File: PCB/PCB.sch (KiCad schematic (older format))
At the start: 32 parts, among them SW1 SW_Push, U1 ATmega32U4-AU, Y1 16MHz

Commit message: finished PCB?
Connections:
- net GND: now also USB1.6 (SHIELD)
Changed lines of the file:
@@
 L power:GND #PWR0113
 U 1 1 608FED04
-P 4750 2150
-F 0 "#PWR0113" H 4750 1900 50  0001 C CNN
-F 1 "GND" H 4755 1977 50  0000 C CNN
-F 2 "" H 4750 2150 50  0001 C CNN
-F 3 "" H 4750 2150 50  0001 C CNN
-	1    4750 2150
-	1    0    0    -1
-$EndComp
-Wire Wire Line
-	4450 2150 4750 2150
+P 5750 2150
+F 0 "#PWR0113" H 5750 1900 50  0001 C CNN
+F 1 "GND" H 5755 1977 50  0000 C CNN
+F 2 "" H 5750 2150 50  0001 C CNN
+F 3 "" H 5750 2150 50  0001 C CNN
+	1    5750 2150
+	1    0    0    -1
+$EndComp
 Text GLabel 2650 4900 0    50   Input ~ 0
 ROW1
@@
 	1    0    0    -1
 $EndComp
-$Comp
-L random-keyboard-parts:Molex-0548190589 USB1
-U 1 1 608F48FD
-P 4150 1950
-F 0 "USB1" V 4687 1917 60  0000 C CNN
-F 1 "Molex-0548190589" V 4581 1917 60  0000 C CNN
-F 2 "random-keyboard-parts:Molex-0548190589" H 4150 1950 60  0001 C CNN
-F 3 "" H 4150 1950 60  0001 C CNN
-	1    4150 1950
-	0    -1   -1   0
-$EndComp
 Text GLabel 8750 3600 2    50   Input ~ 0
 ROW1
@@
 Text GLabel 8750 2700 2    50   Input ~ 0
 ROW0
+$Comp
+L random-keyboard-parts:Molex-0548190589 USB1
+U 1 1 608F48FD
+P 4150 1950
+F 0 "USB1" V 4687 1917 60  0000 C CNN
+F 1 "Molex-0548190589" V 4581 1917 60  0000 C CNN
+F 2 "random-keyboard-parts:Molex-0548190589" H 4150 1950 60  0001 C CNN
+F 3 "" H 4150 1950 60  0001 C CNN
+	1    4150 1950
+	0    -1   -1   0
+$EndComp
+Wire Wire Line
+	4450 1650 5750 1650
+Wire Wire Line
+	5750 1650 5750 2150
+Wire Wire Line
+	4450 2150 5750 2150
+Connection ~ 5750 2150
 $EndSCHEMATC

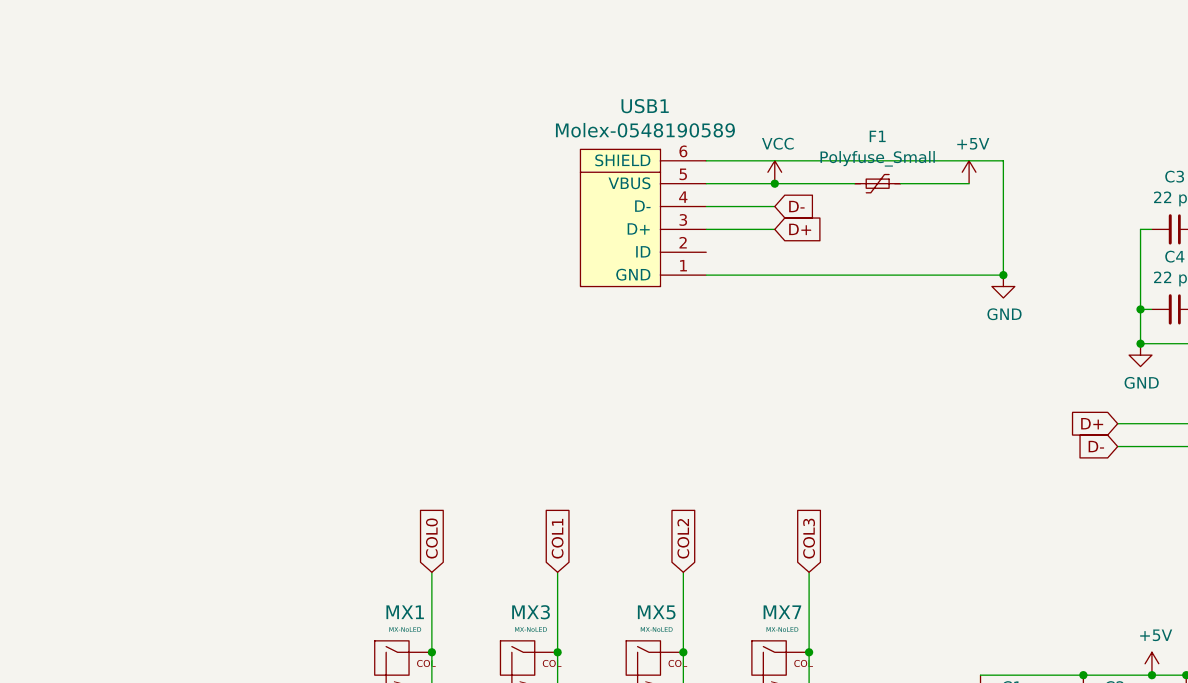
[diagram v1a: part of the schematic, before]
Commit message: major changes: replaced usb with usb type C
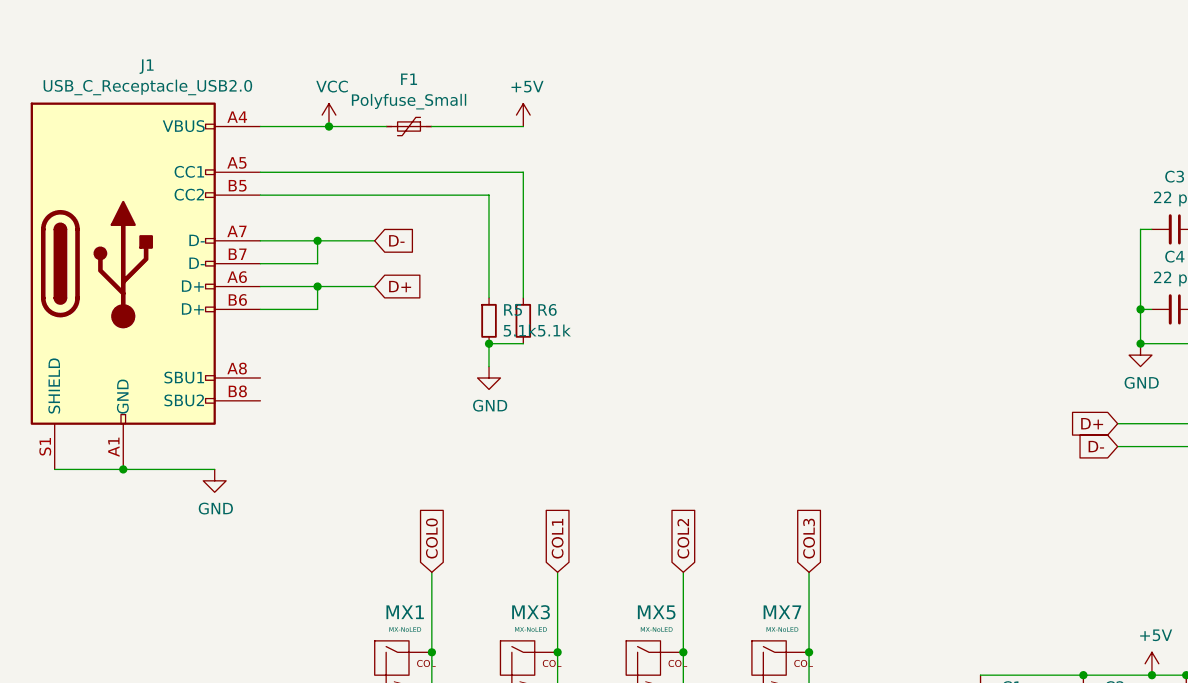
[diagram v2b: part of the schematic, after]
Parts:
- removed USB1: Molex-0548190589, random-keyboard-parts:Molex-0548190589, symbol random-keyboard-parts:Molex-0548190589
- added J1: USB_C_Receptacle_USB2.0, Connector_USB:USB_C_Receptacle_HRO_TYPE-C-31-M-12, symbol Connector:USB_C_Receptacle_USB2.0
- added R5, R6: 5.1k, Resistor_SMD:R_0805_2012Metric, symbol Device:R_Small
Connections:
- net D+: now also J1.A6 (D+), J1.B6 (D+)
- net D-: now also J1.A7 (D-), J1.B7 (D-)
- net GND: now also J1.A1 (GND), J1.A12 (GND), J1.B1 (GND), J1.B12 (GND), J1.S1 (SHIELD), R5.2, R6.2
- net VCC: now also J1.A4 (VBUS), J1.A9 (VBUS), J1.B4 (VBUS), J1.B9 (VBUS)
- new net: J1.A5 (CC1), R6.1
- new net: J1.B5 (CC2), R5.1
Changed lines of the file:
@@
 Text GLabel 6250 2900 0    50   Input ~ 0
 D-
-$Comp
-L Device:Polyfuse_Small F1
-U 1 1 608F77FB
-P 5200 1750
-F 0 "F1" V 4995 1750 50  0000 C CNN
-F 1 "Polyfuse_Small" V 5086 1750 50  0000 C CNN
-F 2 "Fuse:Fuse_1206_3216Metric" H 5250 1550 50  0001 L CNN
-F 3 "~" H 5200 1750 50  0001 C CNN
-	1    5200 1750
-	0    1    1    0
-$EndComp
-$Comp
-L power:+5V #PWR0111
-U 1 1 608F87CE
-P 5600 1750
-F 0 "#PWR0111" H 5600 1600 50  0001 C CNN
-F 1 "+5V" H 5615 1923 50  0000 C CNN
-F 2 "" H 5600 1750 50  0001 C CNN
-F 3 "" H 5600 1750 50  0001 C CNN
-	1    5600 1750
-	1    0    0    -1
-$EndComp
-$Comp
-L power:VCC #PWR0112
-U 1 1 608F9087
-P 4750 1750
-F 0 "#PWR0112" H 4750 1600 50  0001 C CNN
-F 1 "VCC" H 4765 1923 50  0000 C CNN
-F 2 "" H 4750 1750 50  0001 C CNN
-F 3 "" H 4750 1750 50  0001 C CNN
-	1    4750 1750
-	1    0    0    -1
-$EndComp
-Wire Wire Line
-	4450 1750 4750 1750
-Connection ~ 4750 1750
-Wire Wire Line
-	4750 1750 5100 1750
-Wire Wire Line
-	5300 1750 5600 1750
-Text GLabel 4750 1950 2    50   Input ~ 0
-D+
-Text GLabel 4750 1850 2    50   Input ~ 0
-D-
-Wire Wire Line
-	4450 1850 4750 1850
-Wire Wire Line
-	4450 1950 4750 1950
-$Comp
-L power:GND #PWR0113
-U 1 1 608FED04
-P 5750 2150
-F 0 "#PWR0113" H 5750 1900 50  0001 C CNN
-F 1 "GND" H 5755 1977 50  0000 C CNN
-F 2 "" H 5750 2150 50  0001 C CNN
-F 3 "" H 5750 2150 50  0001 C CNN
-	1    5750 2150
-	1    0    0    -1
-$EndComp
 Text GLabel 2650 4900 0    50   Input ~ 0
 ROW1
@@
 ROW0
 $Comp
-L random-keyboard-parts:Molex-0548190589 USB1
-U 1 1 608F48FD
-P 4150 1950
-F 0 "USB1" V 4687 1917 60  0000 C CNN
-F 1 "Molex-0548190589" V 4581 1917 60  0000 C CNN
-F 2 "random-keyboard-parts:Molex-0548190589" H 4150 1950 60  0001 C CNN
-F 3 "" H 4150 1950 60  0001 C CNN
-	1    4150 1950
-	0    -1   -1   0
-$EndComp
-Wire Wire Line
-	4450 1650 5750 1650
-Wire Wire Line
-	5750 1650 5750 2150
-Wire Wire Line
-	4450 2150 5750 2150
-Connection ~ 5750 2150
+L Connector:USB_C_Receptacle_USB2.0 J1
+U 1 1 608F2C24
+P 1900 2100
+F 0 "J1" H 2007 2967 50  0000 C CNN
+F 1 "USB_C_Receptacle_USB2.0" H 2007 2876 50  0000 C CNN
+F 2 "Connector_USB:USB_C_Receptacle_HRO_TYPE-C-31-M-12" H 2050 2100 50  0001 C CNN
+F 3 "https://www.usb.org/sites/default/files/documents/usb_type-c.zip" H 2050 2100 50  0001 C CNN
+	1    1900 2100
+	1    0    0    -1
+$EndComp
+$Comp
+L Device:Polyfuse_Small F1
+U 1 1 608F9DBE
+P 3150 1500
+F 0 "F1" V 2945 1500 50  0000 C CNN
+F 1 "Polyfuse_Small" V 3036 1500 50  0000 C CNN
+F 2 "Fuse:Fuse_1206_3216Metric" H 3200 1300 50  0001 L CNN
+F 3 "~" H 3150 1500 50  0001 C CNN
+	1    3150 1500
+	0    1    1    0
+$EndComp
+$Comp
+L power:VCC #PWR0111
+U 1 1 608FA7E3
+P 2800 1500
+F 0 "#PWR0111" H 2800 1350 50  0001 C CNN
+F 1 "VCC" H 2815 1673 50  0000 C CNN
+F 2 "" H 2800 1500 50  0001 C CNN
+F 3 "" H 2800 1500 50  0001 C CNN
+	1    2800 1500
+	1    0    0    -1
+$EndComp
+$Comp
+L power:+5V #PWR0112
+U 1 1 608FAA63
+P 3650 1500
+F 0 "#PWR0112" H 3650 1350 50  0001 C CNN
+F 1 "+5V" H 3665 1673 50  0000 C CNN
+F 2 "" H 3650 1500 50  0001 C CNN
+F 3 "" H 3650 1500 50  0001 C CNN
+	1    3650 1500
+	1    0    0    -1
+$EndComp
+Wire Wire Line
+	2500 1500 2800 1500
+Connection ~ 2800 1500
+Wire Wire Line
+	2800 1500 3050 1500
+Wire Wire Line
+	3250 1500 3650 1500
+Text GLabel 3000 2000 2    50   Input ~ 0
+D-
+Text GLabel 3000 2200 2    50   Input ~ 0
+D+
+Wire Wire Line
+	2500 2000 2750 2000
+Wire Wire Line
+	2500 2100 2750 2100
+Wire Wire Line
+	2750 2100 2750 2000
+Connection ~ 2750 2000
+Wire Wire Line
+	2750 2000 3000 2000
+Wire Wire Line
+	2500 2200 2750 2200
+Wire Wire Line
+	2500 2300 2750 2300
+Wire Wire Line
+	2750 2300 2750 2200
+Connection ~ 2750 2200
+Wire Wire Line
+	2750 2200 3000 2200
+Wire Wire Line
+	2500 1700 3650 1700
+Wire Wire Line
+	3650 1700 3650 2250
+Wire Wire Line
+	2500 1800 3500 1800
+Wire Wire Line
+	3500 1800 3500 2250
+$Comp
+L Device:R_Small R5
+U 1 1 60917DA8
+P 3500 2350
+F 0 "R5" H 3559 2396 50  0000 L CNN
+F 1 "5.1k" H 3559 2305 50  0000 L CNN
+F 2 "Resistor_SMD:R_0805_2012Metric" H 3500 2350 50  0001 C CNN
+F 3 "~" H 3500 2350 50  0001 C CNN
+	1    3500 2350
+	1    0    0    -1
+$EndComp
+$Comp
+L Device:R_Small R6
+U 1 1 609180C3
+P 3650 2350
+F 0 "R6" H 3709 2396 50  0000 L CNN
+F 1 "5.1k" H 3709 2305 50  0000 L CNN
+F 2 "Resistor_SMD:R_0805_2012Metric" H 3650 2350 50  0001 C CNN
+F 3 "~" H 3650 2350 50  0001 C CNN
+	1    3650 2350
+	1    0    0    -1
+$EndComp
+$Comp
+L power:GND #PWR0113
+U 1 1 609187BA
+P 3500 2550
+F 0 "#PWR0113" H 3500 2300 50  0001 C CNN
+F 1 "GND" H 3505 2377 50  0000 C CNN
+F 2 "" H 3500 2550 50  0001 C CNN
+F 3 "" H 3500 2550 50  0001 C CNN
+	1    3500 2550
+	1    0    0    -1
+$EndComp
+Wire Wire Line
+	3500 2450 3500 2550
+Wire Wire Line
+	3650 2450 3500 2450
+Connection ~ 3500 2450
+$Comp
+L power:GND #PWR0114
+U 1 1 609205B6
+P 2300 3000
+F 0 "#PWR0114" H 2300 2750 50  0001 C CNN
+F 1 "GND" H 2305 2827 50  0000 C CNN
+F 2 "" H 2300 3000 50  0001 C CNN
+F 3 "" H 2300 3000 50  0001 C CNN
+	1    2300 3000
+	1    0    0    -1
+$EndComp
+Wire Wire Line
+	1600 3000 1900 3000
+Connection ~ 1900 3000
+Wire Wire Line
+	1900 3000 2300 3000
 $EndSCHEMATC

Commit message: replaced usb footprint with GCT-usb4085 available in digikey
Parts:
- J1: footprint Connector_USB:USB_C_Receptacle_HRO_TYPE-C-31-M-12 -> Connector_USB:USB_C_Receptacle_GCT_USB4085
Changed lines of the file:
@@
 F 0 "J1" H 2007 2967 50  0000 C CNN
 F 1 "USB_C_Receptacle_USB2.0" H 2007 2876 50  0000 C CNN
-F 2 "Connector_USB:USB_C_Receptacle_HRO_TYPE-C-31-M-12" H 2050 2100 50  0001 C CNN
+F 2 "Connector_USB:USB_C_Receptacle_GCT_USB4085" H 2050 2100 50  0001 C CNN
 F 3 "https://www.usb.org/sites/default/files/documents/usb_type-c.zip" H 2050 2100 50  0001 C CNN
 	1    1900 2100

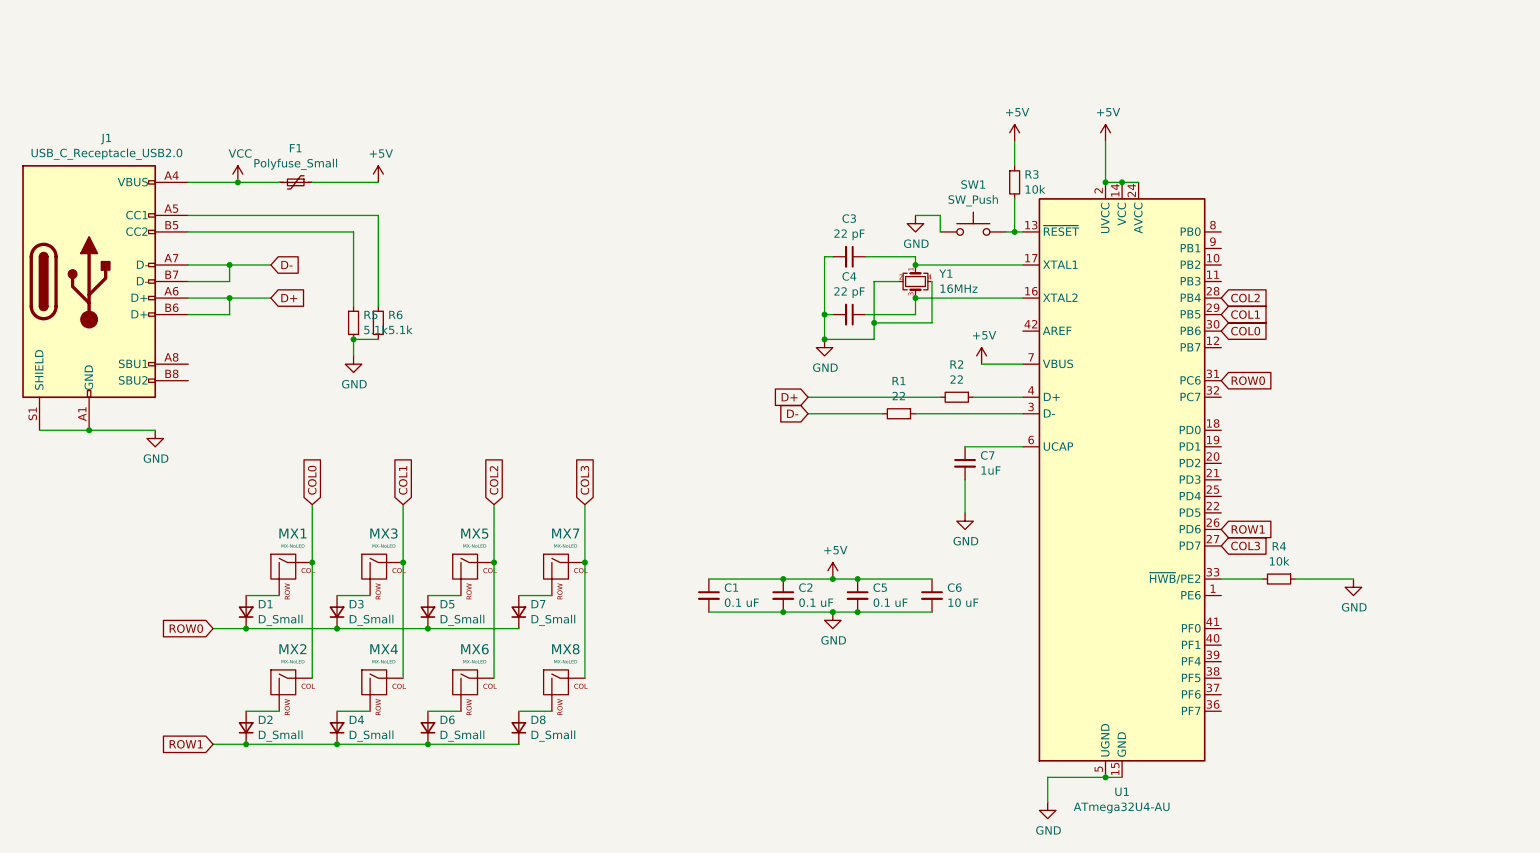
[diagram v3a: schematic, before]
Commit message: replaced mc with ATMEGA32u2
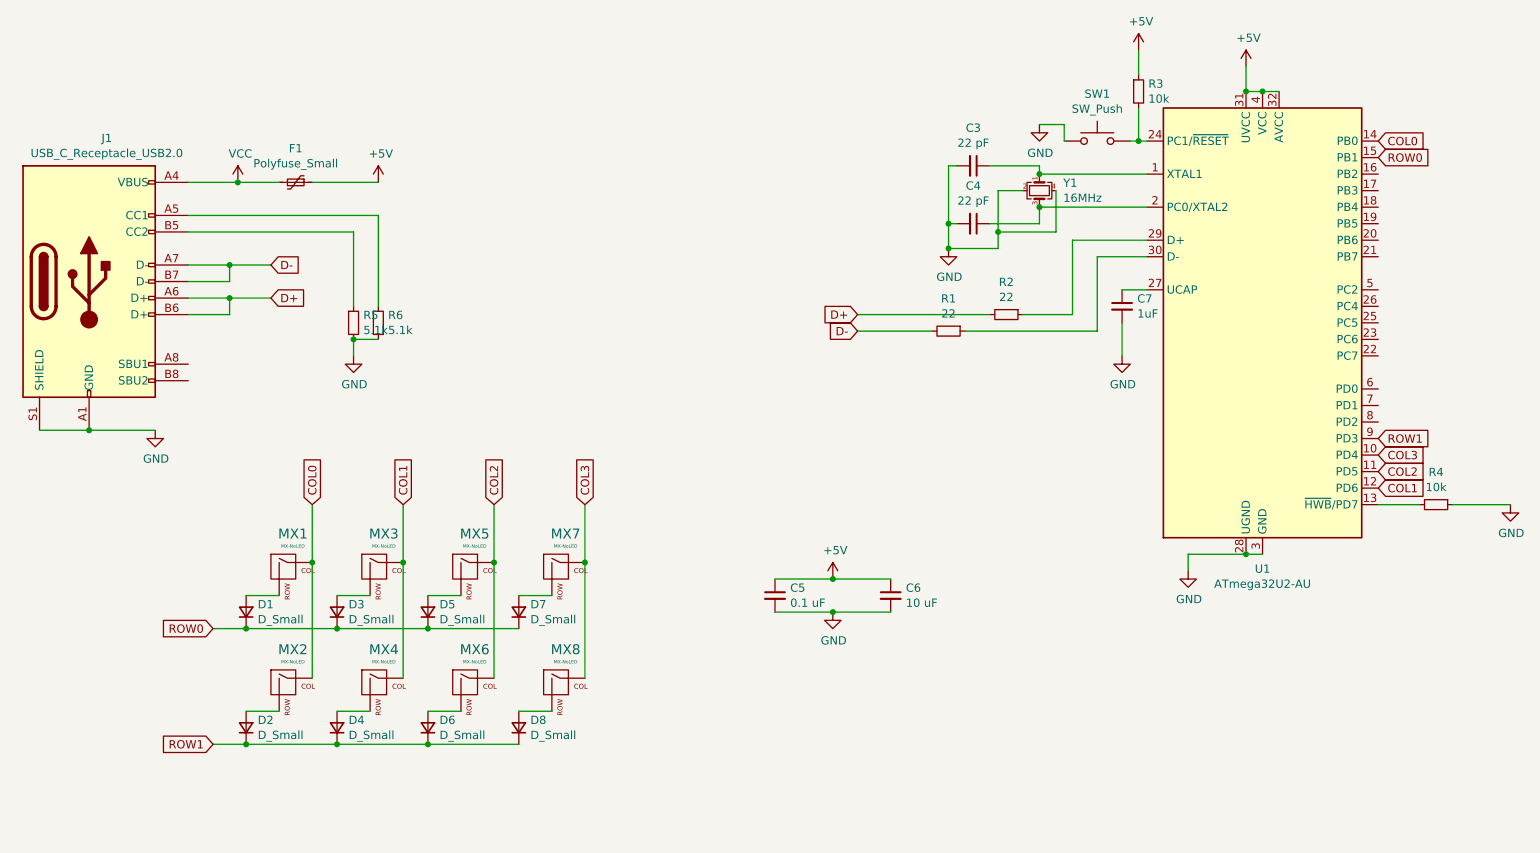
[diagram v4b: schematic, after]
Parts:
- removed C1, C2: 0.1 uF, Capacitor_SMD:C_0805_2012Metric, symbol Device:C_Small
- removed U1: ATmega32U4-AU, Package_QFP:TQFP-44_10x10mm_P0.8mm, symbol MCU_Microchip_ATmega:ATmega32U4-AU
- added U1: ATmega32U2-AU, Package_QFP:TQFP-32_7x7mm_P0.8mm, symbol MCU_Microchip_ATmega:ATmega32U2-AU
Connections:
- net +5V: now also U1.31 (UVCC), U1.32 (AVCC), U1.4 (VCC)
- net COL0: now also U1.14 (PB0)
- net COL1: now also U1.12 (PD6)
- net COL2: now also U1.11 (PD5)
- net COL3: now also U1.10 (PD4)
- net GND: now also U1.28 (UGND), U1.3 (GND)
- net ROW0: now also U1.15 (PB1)
- net ROW1: now also U1.9 (PD3)
- net at R3.2, SW1.2: now also U1.24 (PC1/~RESET)
- net at C4.1, Y1.3: now also U1.2 (PC0/XTAL2)
- net at C3.1, Y1.1: now also U1.1 (XTAL1)
- net at R1.1: now also U1.30 (D-)
- net at R4.2: now also U1.13 (~HWB~/PD7)
- net at R2.1: now also U1.29 (D+)
- net at C7.1: now also U1.27 (UCAP)
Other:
- moved on the sheet: C3, C4, C5, C6, C7, R1, R2, R3, R4, SW1, Y1
